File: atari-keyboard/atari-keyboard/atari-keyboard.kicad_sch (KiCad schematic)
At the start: 20 parts, among them J101 PLAYER 2, J102 PLAYER 1, J103 I2C DISPLAY, U101 Elite-C

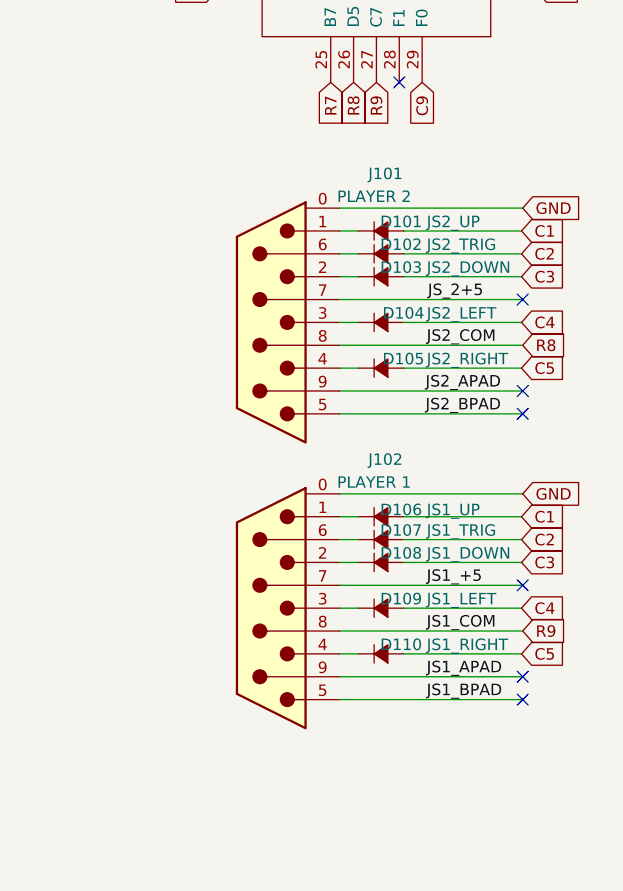
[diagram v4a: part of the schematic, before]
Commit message: Discovered some of the schematic grid was out of alignment
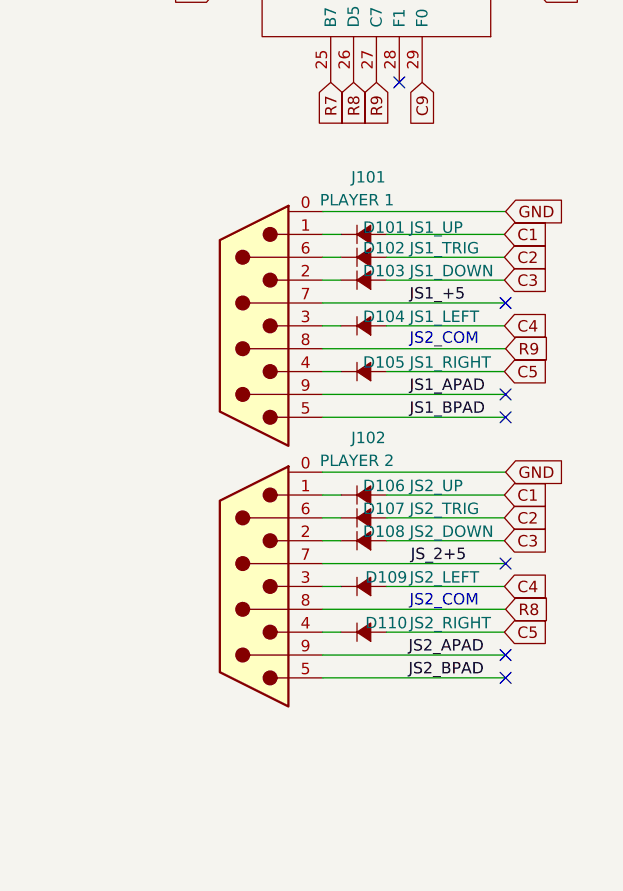
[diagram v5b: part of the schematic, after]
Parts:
- renumbered D106 to D101, D107 to D102, D108 to D103, D109 to D104, D110 to D105, D101 to D106, D102 to D107, D103 to D108, D104 to D109, D105 to D110, J102 to J101, J101 to J102
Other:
- note added: "JS2_COM"
- moved on the sheet: D101, D102, D103, D104, D105, D106, D107, D108, D109, D110, J101, J102
